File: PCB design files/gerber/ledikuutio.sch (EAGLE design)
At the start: 75 parts, among them IC1 ATMEGA328P, IC2 ISO7221A, IC3 74HC595D, Q2 MOSFET-NCHANNELSMD, Q3 16mhz, T1 TIP42, T2 TIP42, T3 TIP42, T4 TIP42, T5 TIP42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

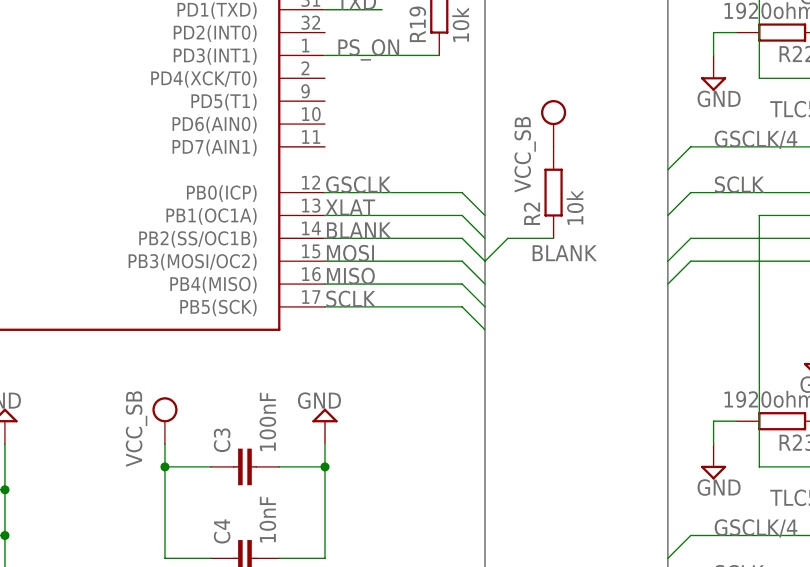
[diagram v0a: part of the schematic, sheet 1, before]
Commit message: Connect MISO and route it. Add up-to-date gerbers and drill files.
MISO was disconnected from the MCU. (doh!). Added newest gerber files and excellon drill files. Updated the pdf files too.
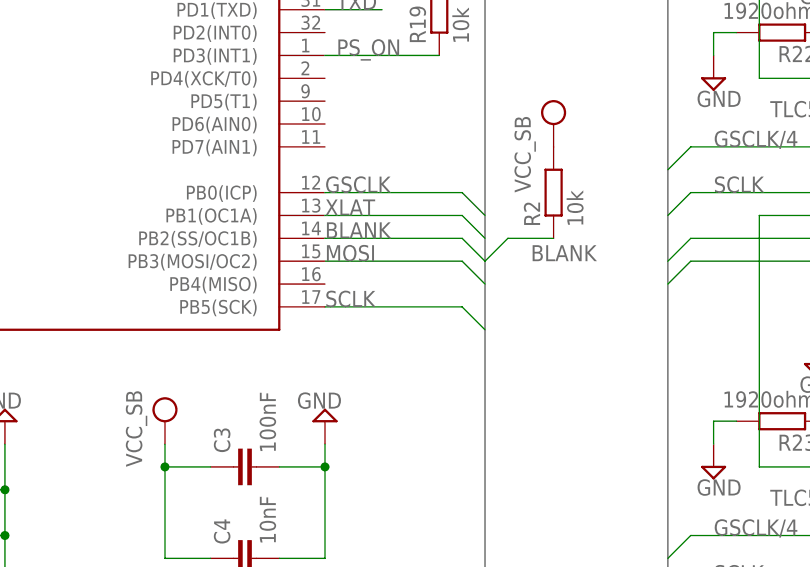
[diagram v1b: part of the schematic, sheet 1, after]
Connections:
- net MISO: no longer IC1.PB4(MISO)
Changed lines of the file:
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@@
 <label x="53.34" y="228.6" size="1.778" layer="95" rot="R90"/>
-</segment>
-<segment>
-<pinref part="IC1" gate="G$1" pin="PB4(MISO)"/>
-<wire x1="116.84" y1="139.7" x2="114.3" y2="142.24" width="0.1524" layer="91"/>
-<wire x1="114.3" y1="142.24" x2="99.06" y2="142.24" width="0.1524" layer="91"/>
-<label x="99.06" y="142.24" size="1.778" layer="95"/>
 </segment>
 </net>
